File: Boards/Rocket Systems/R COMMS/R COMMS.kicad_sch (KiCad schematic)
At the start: 49 parts, among them IC1 NSVT30010MXV6T1G, IC2 NSVT30010MXV6T1G, J2 22285061, J4 MEM2061-01-188-00-A_REVA, J5 1190297, J6 SMARA_CONNECTOR, U3 SX1280IMLTRT, U4 NRF21540-QDAA-R, U6 MAX485CSA+T, U7 VLMKG3400-GS08, U8 STLM20DD9F, U9 VLMKG3400-GS08

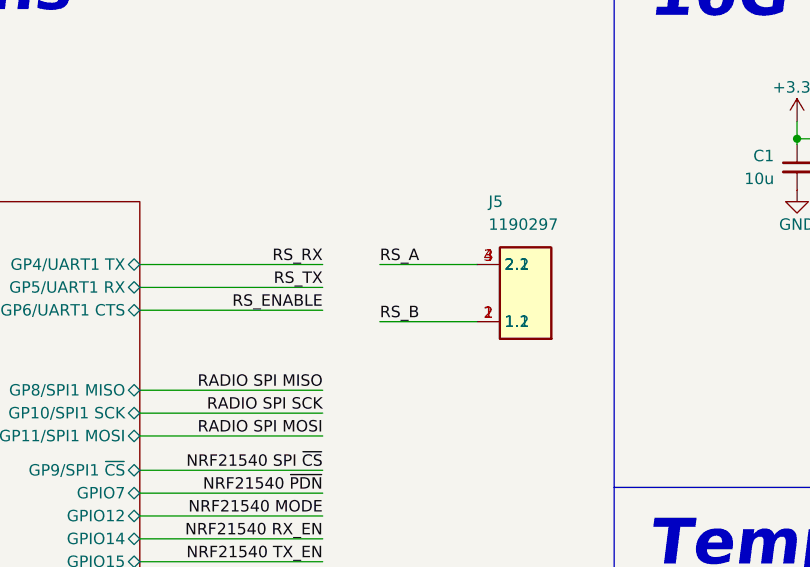
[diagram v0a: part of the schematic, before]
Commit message: 3D Symbols Update and R Comms PCB layout (1)
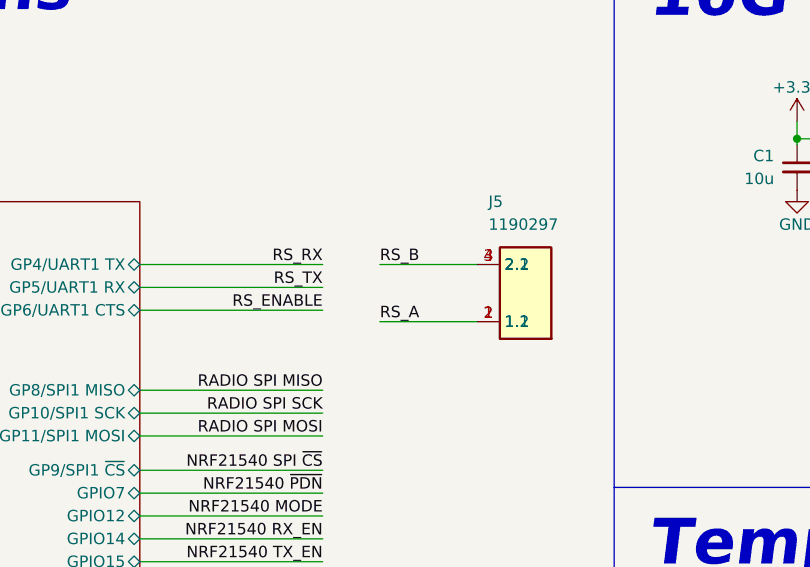
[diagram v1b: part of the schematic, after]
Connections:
- net RS_A: now also J5.1 (1.1), J5.2 (1.2); no longer J5.3 (2.1), J5.4 (2.2)
- net RS_B: now also J5.3 (2.1), J5.4 (2.2); no longer J5.1 (1.1), J5.2 (1.2)

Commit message: 3D models update
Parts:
- CR2, CR3: footprint LED-Yellow_VLMY1300-GS08:LED_VISHAY_VLMX1300_VIS -> LEDC1608X100N
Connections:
- net RS_A: now also J5.3 (2.1), J5.4 (2.2); no longer J5.1 (1.1), J5.2 (1.2)
- net RS_B: now also J5.1 (1.1), J5.2 (1.2); no longer J5.3 (2.1), J5.4 (2.2)
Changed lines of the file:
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@@
 	(wire
 		(pts
+			(xy 130.81 49.53) (xy 141.605 49.53)
+		)
+		(stroke
+			(width 0)
+			(type default)
+		)
+	)
+	(wire
+		(pts
 			(xy 290.83 167.005) (xy 300.355 167.005)
 		)
@@
 		)
 	)
-	(wire
-		(pts
-			(xy 130.81 49.53) (xy 141.605 49.53)
-		)
-		(stroke
-			(width 0)
-			(type default)
-		)
-	)
 	(polyline
 		(pts
@@
 	(wire
 		(pts
+			(xy 130.81 55.88) (xy 141.605 55.88)
+		)
+		(stroke
+			(width 0)
+			(type default)
+		)
+	)
+	(wire
+		(pts
 			(xy 280.67 43.18) (xy 280.67 46.355)
 		)
@@
 	(wire
 		(pts
-			(xy 130.81 55.88) (xy 141.605 55.88)
-		)
-		(stroke
-			(width 0)
-			(type default)
-		)
-	)
-	(wire
-		(pts
 			(xy 124.46 66.04) (xy 104.14 66.04)
 		)
@@
 		)
 	)
+	(label "RS_A"
+		(at 130.81 49.53 0)
+		(effects
+			(font
+				(size 1.27 1.27)
+			)
+			(justify left bottom)
+		)
+	)
 	(label "SX1280 SPI ~{CS}"
 		(at 168.275 180.975 180)
@@
 		)
 	)
-	(label "RS_B"
-		(at 130.81 49.53 0)
-		(effects
-			(font
-				(size 1.27 1.27)
-			)
-			(justify left bottom)
-		)
-	)
 	(label "SD-Card SPI MISO"
 		(at 40.005 85.09 0)
@@
 		)
 	)
+	(label "RS_B"
+		(at 130.81 55.88 0)
+		(effects
+			(font
+				(size 1.27 1.27)
+			)
+			(justify left bottom)
+		)
+	)
 	(label "NRF21540 TX_EN"
 		(at 124.46 82.55 180)
@@
 		)
 	)
-	(label "RS_A"
-		(at 130.81 55.88 0)
-		(effects
-			(font
-				(size 1.27 1.27)
-			)
-			(justify left bottom)
-		)
-	)
 	(label "SX1280 ~{RST}"
 		(at 124.46 99.06 180)
@@
 			)
 		)
-		(property "Footprint" "LED-Yellow_VLMY1300-GS08:LED_VISHAY_VLMX1300_VIS"
+		(property "Footprint" "LEDC1608X100N"
 			(at 346.71 40.005 0)
 			(effects
@@
 	)
 	(symbol
+		(lib_name "VLMY1300-GS08_1")
 		(lib_id "VLMY1300-GS08:VLMY1300-GS08")
 		(at 361.315 40.64 90)
@@
 			)
 		)
-		(property "Footprint" "LED-Yellow_VLMY1300-GS08:LED_VISHAY_VLMX1300_VIS"
+		(property "Footprint" "LEDC1608X100N"
 			(at 361.315 40.64 0)
 			(effects
@@
 		(fields_autoplaced yes)
 		(property "Reference" "IC1"
-			(at 320.04 50.165 0)
+			(at 320.04 49.53 0)
 			(effects
 				(font
@@
 		)
 		(property "Value" "NSVT30010MXV6T1G"
-			(at 320.04 52.705 0)
+			(at 320.04 52.07 0)
 			(effects
 				(font

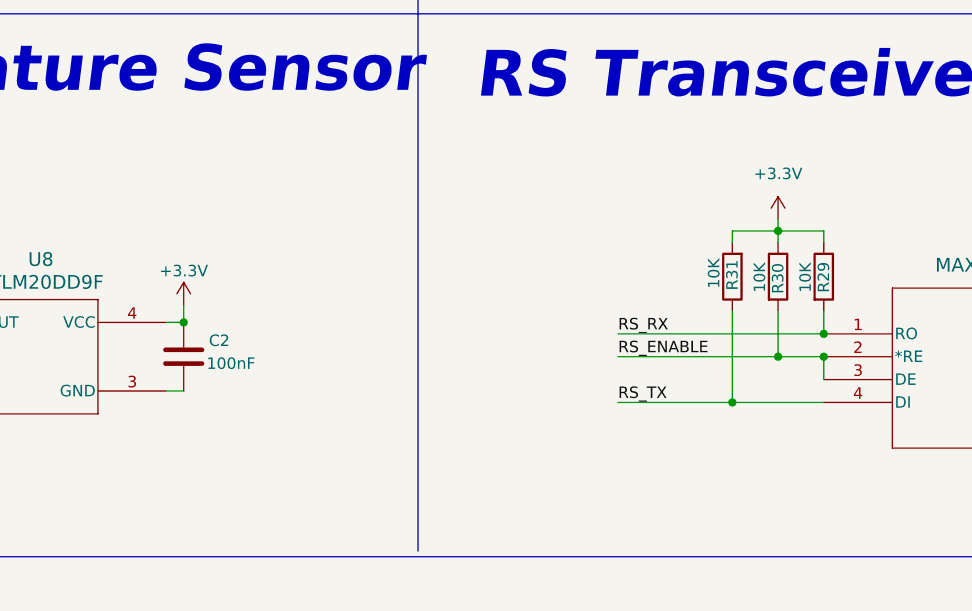
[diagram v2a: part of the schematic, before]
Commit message: R COMMS layout placement update
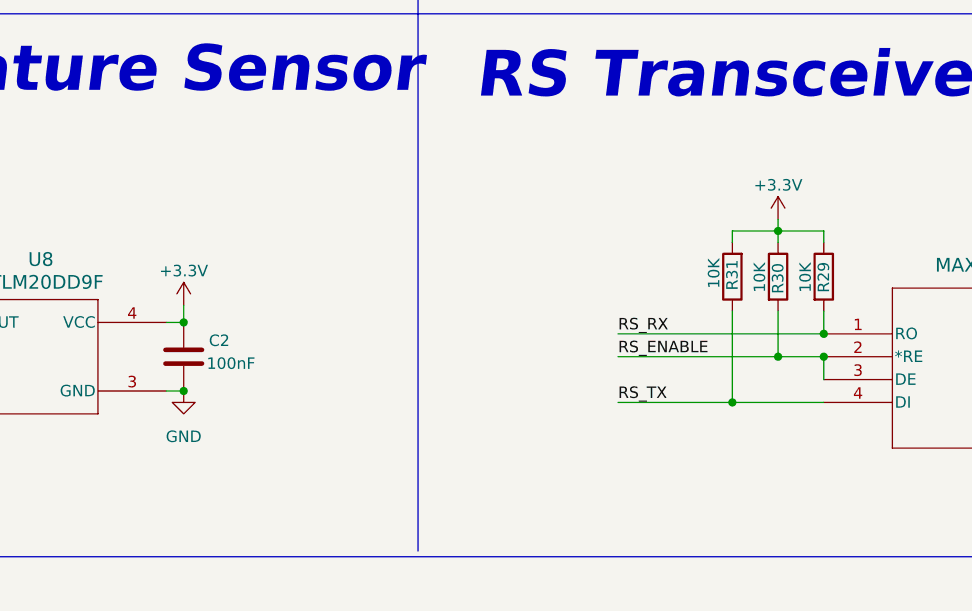
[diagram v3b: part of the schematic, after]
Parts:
- CR2, CR3: footprint LEDC1608X100N -> LED-Yellow_VLMY1300-GS08:LEDC1608X100N
- J4: Description_1 10 (8 + 2) Position Card Connector microSD Surface Mount, Right Angle Gold -> 10 (8 + 2) Position Card Connector microSD Surface Mount, Right Angle Gold
- J6: footprint SMARACONNECTOR -> Side Angle SMA:SMARACONNECTOR
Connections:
- net GND: now also C2.2, U8.3 (GND)
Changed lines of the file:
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@@
 	)
 	(junction
+		(at 214.63 116.205)
+		(diameter 0)
+		(color 0 0 0 0)
+	)
+	(junction
 		(at 93.345 212.725)
 		(diameter 0)
@@
 			)
 		)
-		(property "Footprint" "LEDC1608X100N"
+		(property "Footprint" "LED-Yellow_VLMY1300-GS08:LEDC1608X100N"
 			(at 346.71 40.005 0)
 			(effects
@@
 	)
 	(symbol
-		(lib_name "VLMY1300-GS08_1")
 		(lib_id "VLMY1300-GS08:VLMY1300-GS08")
 		(at 361.315 40.64 90)
@@
 			)
 		)
-		(property "Footprint" "LEDC1608X100N"
+		(property "Footprint" "LED-Yellow_VLMY1300-GS08:LEDC1608X100N"
 			(at 361.315 40.64 0)
 			(effects
@@
 	)
 	(symbol
+		(lib_id "power:+3.3V")
+		(at 280.67 97.155 0)
+		(unit 1)
+		(exclude_from_sim no)
+		(in_bom yes)
+		(on_board yes)
+		(dnp no)
+		(property "Reference" "#PWR069"
+			(at 280.67 100.965 0)
+			(effects
+				(font
+					(size 1.27 1.27)
+				)
+				(hide yes)
+			)
+		)
+		(property "Value" "+3.3V"
+			(at 280.67 93.345 0)
+			(effects
+				(font
+					(size 1.27 1.27)
+				)
+			)
+		)
+		(property "Footprint" ""
+			(at 280.67 97.155 0)
+			(effects
+				(font
+					(size 1.27 1.27)
+				)
+				(hide yes)
+			)
+		)
+		(property "Datasheet" ""
+			(at 280.67 97.155 0)
+			(effects
+				(font
+					(size 1.27 1.27)
+				)
+				(hide yes)
+			)
+		)
+		(property "Description" "Power symbol creates a global label with name \"+3.3V\""
+			(at 280.67 97.155 0)
+			(effects
+				(font
+					(size 1.27 1.27)
+				)
+				(hide yes)
+			)
+		)
+		(pin "1"
+		)
+		(instances
+			(project "R COMMS"
+				(path "/169b1789-9bea-4709-830d-1c7983087293"
+					(reference "#PWR069")
+					(unit 1)
+				)
+			)
+		)
+	)
+	(symbol
 		(lib_id "power:GND")
 		(at 177.165 41.275 0)
@@
 	(symbol
 		(lib_id "power:GND")
+		(at 214.63 116.205 0)
+		(unit 1)
+		(exclude_from_sim no)
+		(in_bom yes)
+		(on_board yes)
+		(dnp no)
+		(fields_autoplaced yes)
+		(property "Reference" "#PWR066"
+			(at 214.63 122.555 0)
+			(effects
+				(font
+					(size 1.27 1.27)
+				)
+				(hide yes)
+			)
+		)
+		(property "Value" "GND"
+			(at 214.63 121.285 0)
+			(effects
+				(font
+					(size 1.27 1.27)
+				)
+			)
+		)
+		(property "Footprint" ""
+			(at 214.63 116.205 0)
+			(effects
+				(font
+					(size 1.27 1.27)
+				)
+				(hide yes)
+			)
+		)
+		(property "Datasheet" ""
+			(at 214.63 116.205 0)
+			(effects
+				(font
+					(size 1.27 1.27)
+				)
+				(hide yes)
+			)
+		)
+		(property "Description" "Power symbol creates a global label with name \"GND\" , ground"
+			(at 214.63 116.205 0)
+			(effects
+				(font
+					(size 1.27 1.27)
+				)
+				(hide yes)
+			)
+		)
+		(pin "1"
+		)
+		(instances
+			(project "R COMMS"
+				(path "/169b1789-9bea-4709-830d-1c7983087293"
+					(reference "#PWR066")
+					(unit 1)
+				)
+			)
+		)
+	)
+	(symbol
+		(lib_id "power:GND")
 		(at 311.785 180.975 0)
 		(unit 1)
@@
 	)
 	(symbol
-		(lib_id "power:+3.3V")
-		(at 280.67 97.155 0)
-		(mirror y)
-		(unit 1)
-		(exclude_from_sim no)
-		(in_bom yes)
-		(on_board yes)
-		(dnp no)
-		(fields_autoplaced yes)
-		(property "Reference" "#PWR066"
-			(at 280.67 100.965 0)
-			(effects
-				(font
-					(size 1.27 1.27)
-				)
-				(hide yes)
-			)
-		)
-		(property "Value" "+3.3V"
-			(at 280.67 92.075 0)
-			(effects
-				(font
-					(size 1.27 1.27)
-				)
-			)
-		)
-		(property "Footprint" "RES_0402:RES_0402"
-			(at 351.282 114.3 90)
-			(effects
-				(font
-					(size 1.27 1.27)
-				)
-				(hide yes)
-			)
-		)
-		(property "Datasheet" ""
-			(at 280.67 97.155 0)
-			(effects
-				(font
-					(size 1.27 1.27)
-				)
-				(hide yes)
-			)
-		)
-		(property "Description" "Power symbol creates a global label with name \"+3.3V\""
-			(at 280.67 97.155 0)
-			(effects
-				(font
-					(size 1.27 1.27)
-				)
-				(hide yes)
-			)
-		)
-		(pin "1"
-		)
-		(instances
-			(project "R COMMS"
-				(path "/169b1789-9bea-4709-830d-1c7983087293"
-					(reference "#PWR066")
-					(unit 1)
-				)
-			)
-		)
-	)
-	(symbol
 		(lib_id "Device:C_Small")
 		(at 300.355 164.465 0)
@@
 			)
 		)
-		(property "Description_1" "\n                        \n                            10 (8 + 2) Position Card Connector microSD Surface Mount, Right Angle Gold\n                        \n"
+		(property "Description_1" "10 (8 + 2) Position Card Connector microSD Surface Mount, Right Angle Gold"
 			(at 205.105 48.26 0)
 			(effects
@@
 	)
 	(symbol
-		(lib_name "SMARA_CONNECTOR_1")
 		(lib_id "SMARA_CONNECTOR:SMARA_CONNECTOR")
 		(at 327.025 173.355 0)
@@
 			)
 		)
-		(property "Footprint" "SMARACONNECTOR"
+		(property "Footprint" "Side Angle SMA:SMARACONNECTOR"
 			(at 310.515 268.275 0)
 			(effects

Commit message: full update on RCOMMS layout
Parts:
- removed IC1: NSVT30010MXV6T1G, 2 PNP:SOT-563_1P3X1P7_ONS, symbol NSVT30010MXV6T1G:NSVT30010MXV6T1G
- removed J5: 1190297, LPT Conn 2 Entradas:1190297, symbol 1190297:1190297
- removed R12, R14: 100, Resistor-0402:RES_0402, symbol Device:R
- removed R31: 10K, Resistor-0402:RES_0402, symbol Device:R
- removed S5: TL1017AABF160QG, E-Switch_Small:TL1017AABF160QG, symbol TL1017AABF160QG:TL1017AABF160QG
- removed U6: MAX485CSA+T, RS Transceiver:21-0041-3-M_90-0096-8L_MXM, symbol RS_Transceiver:MAX485CSA+T
- removed U7: VLMKG3400-GS08, VLMKG3400-GS08:SMT_00-GS08_VIS, symbol VLMKG3400-GS08:VLMKG3400-GS08
- added C29, C40: 4.7u, Capacitor-0402:Capacitor_0402, symbol Device:C_Small
- added C30, C31, C37, C38, C39, C41: 100nF, Capacitor-0402:Capacitor_0402, symbol Device:C
- added H1, H2, H3, H4: MountingHole, MountingHole:MountingHole_3.2mm_M3_ISO7380_Pad_TopBottom, symbol Mechanical:MountingHole
- added IC1: BC846BLT1G, BJT NPN:SOT96P237X111-3N, symbol BC846BLT1G:BC846BLT1G
- added IC3: THVD2412VDR, THVD2412VDR:SOIC127P600X175-14N, symbol THVD2412VDR:THVD2412VDR
- added J5: 5023520600, 5023520600:CONN06_502352_MOL, symbol 5023520600:5023520600
- added JP1: Jumper_2_Bridged, Jumper:SolderJumper-2_P1.3mm_Open_RoundedPad1.0x1.5mm, symbol Jumper:Jumper_2_Bridged
- added LS1: PKLCS1212E20A0-R1, PKLCS1212E20A0-R1:PKLCS1212E20A0-R1, symbol PKLCS1212E20A0-R1:PKLCS1212E20A0-R1
- added MP1, MP2, MP3, MP4: S0991-46R, S0991-46R:S099146R, symbol S0991-46R:S0991-46R
- added R17, R18: 1k, Resistor-0402:RES_0402, symbol Device:R
- added R21, R22, R23: 10k, Resistor-0402:RES_0402, symbol Device:R
- added R24, R25: 120, Resistor-0402:RES_0402, symbol Device:R
- added U6, U7: IP4220CZ6, IP4220CZ6:SOT457_NEX, symbol IP4220CZ6F:IP4220CZ6
- R26: value 120 -> 523
- R27, R28: value 20K -> 523
- R29: value 10K -> 523
- R30: value 10K -> 10k
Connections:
- net +3.3V: now also C30.1, C37.1, C41.1, IC3.1 (VIO), R21.1, R23.1, U7.5 (VP); no longer R29.1
- net +5V: now also R28.1, C29.2, C31.2, C38.2, C39.1, C40.2, IC3.14 (VCC), LS1.P, R18.1, U6.5 (VP)
- net GND: now also J2.2, R26.2, R29.2, C29.1, C30.2, C31.1, C37.2, C38.1, C39.2, C40.1, C41.2, IC1.2 (E), IC3.3 (~{RE}), IC3.6 (GND), JP1.1 (A), MP1.1, MP1.2, MP1.3, MP2.1, MP2.2, MP2.3, MP3.1, MP3.2, MP3.3, MP4.1, MP4.2, MP4.3, R22.2, U6.2 (GND), U7.2 (GND); no longer J2.6, R28.2
- net OBC UART CTS: now also J2.5, U7.6 (IO4); no longer J2.4
- net OBC UART RTS: now also J2.6, U7.4 (IO3); no longer J2.5
- net OBC UART RX: now also J2.4, U7.3 (IO2); no longer J2.3
- net OBC UART TX: now also J2.3, U7.1 (IO1); no longer J2.2
- net RS_RX: now also IC3.2 (R), R21.2; no longer R29.2
- net RS_TX: now also IC3.5 (D)
- net at R16.1: now also JP1.2 (B)
- net RS_A renamed RS-RX_DP
- net RS-RX_DP: now also IC3.12 (A), J5.6, R24.2, U6.6 (IO4); no longer R26.2
- net RS_B renamed RS-RX_DN
- net RS-RX_DN: now also IC3.11 (B), J5.5, R24.1, U6.4 (IO3); no longer R28.1
- net RS_ENABLE: no longer names the net of R30.2
- net RS_ENABLE: now also IC3.4 (DE)
- new net: IC3.8 (SLR), R22.1, R23.2
- new net: IC1.3 (C), LS1.N, R18.2
- new net: IC1.1 (B), R17.1
- new net Buzzer: R17.2
- new net Pyro Drogue: J5.2
- new net Pyro Main Chute: J5.1
- new net RS-TX_DN: IC3.10 (Z), J5.4, R25.1, R29.1, U6.1 (IO1)
- new net RS-TX_DP: IC3.9 (Y), J5.3, R25.2, R28.2, U6.3 (IO2)
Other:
- sheet RP2040 ports: added GP6/PWM3 A; removed GP6/UART1 CTS
- note added: "LED & Buzzer Drivers"
- note added: "RFI Shield Clips"
- note added: "RS Transceiver (MASTER)"
- note added: "Toggled to 1Mbps"
- note removed: "LED Driver"
- note removed: "RS Transceiver"
- moved on the sheet: C1, C19, C2, C20, CR2, CR3, IC2, J2, J4, R10, R11, R15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
